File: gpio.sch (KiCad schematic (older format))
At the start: 33 parts, among them J3 Pro Bus, J7 PMOD1, J8 PMOD, SW1 SW_Push, SW2 SW_Push

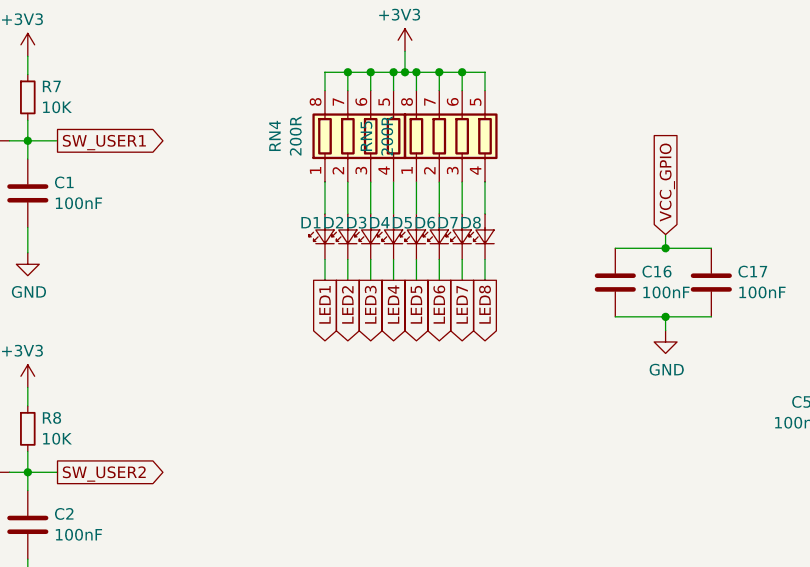
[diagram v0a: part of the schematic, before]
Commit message: component placement
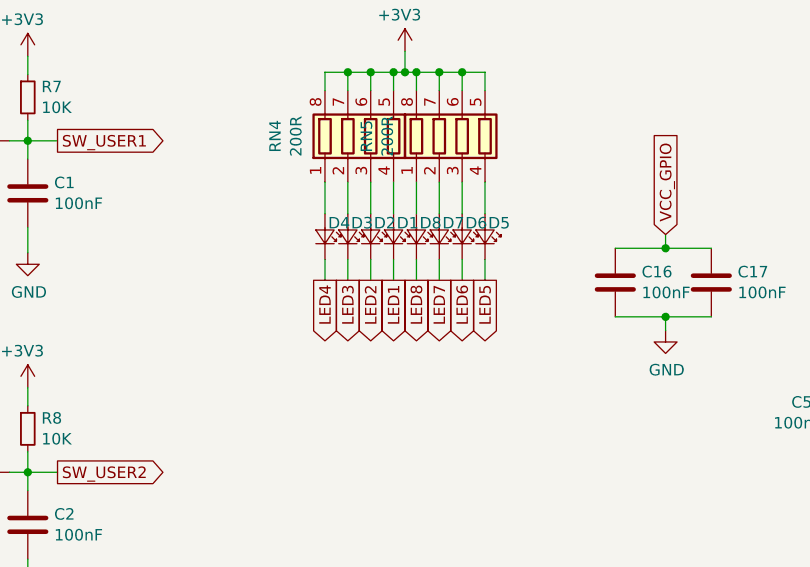
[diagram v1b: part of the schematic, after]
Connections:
- net at D5.2 (A): now also RN5.4 (R4.1); no longer RN5.1 (R1.1)
- net at D6.2 (A): now also RN5.3 (R3.1); no longer RN5.2 (R2.1)
- net at D7.2 (A): now also RN5.2 (R2.1); no longer RN5.3 (R3.1)
- net at D8.2 (A): now also RN5.1 (R1.1); no longer RN5.4 (R4.1)
- net at RN4.1 (R1.1): now also D4.2 (A); no longer D1.2 (A)
- net at RN4.2 (R2.1): now also D3.2 (A); no longer D2.2 (A)
- net at RN4.3 (R3.1): now also D2.2 (A); no longer D3.2 (A)
- net at RN4.4 (R4.1): now also D1.2 (A); no longer D4.2 (A)
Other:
- moved on the sheet: D1, D2, D3, D4, D5, D6, D7, D8
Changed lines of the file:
@@
 $Descr A4 11693 8268
 encoding utf-8
-Sheet 4 6
+Sheet 5 6
 Title ""
 Date ""
@@
 L Device:LED_Small D?
 U 1 1 5D1B162E
-P 3280 1720
+P 3580 1720
 AR Path="/5CFABACD/5D1B162E" Ref="D?"  Part="1"
 AR Path="/5CF9C1ED/5D1B162E" Ref="D5"  Part="1"
-F 0 "D5" V 3340 1830 50  0000 R CNN
+F 0 "D5" V 3640 1830 50  0000 R CNN
+F 1 "Blue" V 3535 1652 50  0001 R CNN
+F 2 "LED_SMD:LED_0603_1608Metric_Pad1.05x0.95mm_HandSolder" V 3580 1720 50  0001 C CNN
+F 3 "~" V 3580 1720 50  0001 C CNN
+	1    3580 1720
+	0    1    -1   0
+$EndComp
+$Comp
+L Device:LED_Small D?
+U 1 1 5D1B1634
+P 3480 1720
+AR Path="/5CFABACD/5D1B1634" Ref="D?"  Part="1"
+AR Path="/5CF9C1ED/5D1B1634" Ref="D6"  Part="1"
+F 0 "D6" V 3540 1830 50  0000 R CNN
+F 1 "Blue" V 3435 1652 50  0001 R CNN
+F 2 "LED_SMD:LED_0603_1608Metric_Pad1.05x0.95mm_HandSolder" V 3480 1720 50  0001 C CNN
+F 3 "~" V 3480 1720 50  0001 C CNN
+	1    3480 1720
+	0    1    -1   0
+$EndComp
+$Comp
+L Device:LED_Small D?
+U 1 1 5D1B163A
+P 3380 1720
+AR Path="/5CFABACD/5D1B163A" Ref="D?"  Part="1"
+AR Path="/5CF9C1ED/5D1B163A" Ref="D7"  Part="1"
+F 0 "D7" V 3440 1830 50  0000 R CNN
+F 1 "Blue" V 3335 1652 50  0001 R CNN
+F 2 "LED_SMD:LED_0603_1608Metric_Pad1.05x0.95mm_HandSolder" V 3380 1720 50  0001 C CNN
+F 3 "~" V 3380 1720 50  0001 C CNN
+	1    3380 1720
+	0    1    -1   0
+$EndComp
+$Comp
+L Device:LED_Small D?
+U 1 1 5D1B1640
+P 3280 1720
+AR Path="/5CFABACD/5D1B1640" Ref="D?"  Part="1"
+AR Path="/5CF9C1ED/5D1B1640" Ref="D8"  Part="1"
+F 0 "D8" V 3340 1830 50  0000 R CNN
 F 1 "Blue" V 3235 1652 50  0001 R CNN
 F 2 "LED_SMD:LED_0603_1608Metric_Pad1.05x0.95mm_HandSolder" V 3280 1720 50  0001 C CNN
 F 3 "~" V 3280 1720 50  0001 C CNN
 	1    3280 1720
-	0    -1   -1   0
-$EndComp
-$Comp
-L Device:LED_Small D?
-U 1 1 5D1B1634
-P 3380 1720
-AR Path="/5CFABACD/5D1B1634" Ref="D?"  Part="1"
-AR Path="/5CF9C1ED/5D1B1634" Ref="D6"  Part="1"
-F 0 "D6" V 3440 1830 50  0000 R CNN
-F 1 "Blue" V 3335 1652 50  0001 R CNN
-F 2 "LED_SMD:LED_0603_1608Metric_Pad1.05x0.95mm_HandSolder" V 3380 1720 50  0001 C CNN
-F 3 "~" V 3380 1720 50  0001 C CNN
-	1    3380 1720
-	0    -1   -1   0
-$EndComp
-$Comp
-L Device:LED_Small D?
-U 1 1 5D1B163A
-P 3480 1720
-AR Path="/5CFABACD/5D1B163A" Ref="D?"  Part="1"
-AR Path="/5CF9C1ED/5D1B163A" Ref="D7"  Part="1"
-F 0 "D7" V 3540 1830 50  0000 R CNN
-F 1 "Blue" V 3435 1652 50  0001 R CNN
-F 2 "LED_SMD:LED_0603_1608Metric_Pad1.05x0.95mm_HandSolder" V 3480 1720 50  0001 C CNN
-F 3 "~" V 3480 1720 50  0001 C CNN
-	1    3480 1720
-	0    -1   -1   0
-$EndComp
-$Comp
-L Device:LED_Small D?
-U 1 1 5D1B1640
-P 3580 1720
-AR Path="/5CFABACD/5D1B1640" Ref="D?"  Part="1"
-AR Path="/5CF9C1ED/5D1B1640" Ref="D8"  Part="1"
-F 0 "D8" V 3640 1830 50  0000 R CNN
-F 1 "Blue" V 3535 1652 50  0001 R CNN
-F 2 "LED_SMD:LED_0603_1608Metric_Pad1.05x0.95mm_HandSolder" V 3580 1720 50  0001 C CNN
-F 3 "~" V 3580 1720 50  0001 C CNN
-	1    3580 1720
-	0    -1   -1   0
+	0    1    -1   0
 $EndComp
 Wire Wire Line
@@
 Wire Wire Line
 	3580 1620 3580 1480
-Text GLabel 3180 1910 3    50   Output ~ 0
+Text GLabel 2880 1910 3    50   Output ~ 0
 LED4
 Wire Wire Line
-	3180 1820 3180 1910
+	2880 1820 2880 1910
+Text GLabel 3580 1910 3    50   Output ~ 0
+LED5
+Wire Wire Line
+	3580 1820 3580 1910
+Text GLabel 3480 1910 3    50   Output ~ 0
+LED6
+Wire Wire Line
+	3480 1820 3480 1910
+Text GLabel 3380 1910 3    50   Output ~ 0
+LED7
+Wire Wire Line
+	3380 1820 3380 1910
 Text GLabel 3280 1910 3    50   Output ~ 0
-LED5
+LED8
 Wire Wire Line
 	3280 1820 3280 1910
-Text GLabel 3380 1910 3    50   Output ~ 0
-LED6
-Wire Wire Line
-	3380 1820 3380 1910
-Text GLabel 3480 1910 3    50   Output ~ 0
-LED7
-Wire Wire Line
-	3480 1820 3480 1910
-Text GLabel 3580 1910 3    50   Output ~ 0
-LED8
-Wire Wire Line
-	3580 1820 3580 1910
 Wire Wire Line
 	3580 1000 3580 1080
@@
 	2880 1080 2880 1000
 Wire Wire Line
+	2980 1820 2980 1910
+Text GLabel 2980 1910 3    50   Output ~ 0
+LED3
+Wire Wire Line
 	3080 1820 3080 1910
 Text GLabel 3080 1910 3    50   Output ~ 0
-LED3
-Wire Wire Line
-	2980 1820 2980 1910
-Text GLabel 2980 1910 3    50   Output ~ 0
 LED2
 Wire Wire Line
-	2880 1820 2880 1910
-Text GLabel 2880 1910 3    50   Output ~ 0
+	3180 1820 3180 1910
+Text GLabel 3180 1910 3    50   Output ~ 0
 LED1
 Wire Wire Line
@@
 L Device:LED_Small D?
 U 1 1 5D1B16E7
-P 3180 1720
+P 2880 1720
 AR Path="/5CFABACD/5D1B16E7" Ref="D?"  Part="1"
 AR Path="/5CF9C1ED/5D1B16E7" Ref="D4"  Part="1"
-F 0 "D4" V 3240 1830 50  0000 R CNN
+F 0 "D4" V 2940 1830 50  0000 R CNN
+F 1 "Blue" V 2835 1652 50  0001 R CNN
+F 2 "LED_SMD:LED_0603_1608Metric_Pad1.05x0.95mm_HandSolder" V 2880 1720 50  0001 C CNN
+F 3 "~" V 2880 1720 50  0001 C CNN
+	1    2880 1720
+	0    1    -1   0
+$EndComp
+$Comp
+L Device:LED_Small D?
+U 1 1 5D1B16ED
+P 2980 1720
+AR Path="/5CFABACD/5D1B16ED" Ref="D?"  Part="1"
+AR Path="/5CF9C1ED/5D1B16ED" Ref="D3"  Part="1"
+F 0 "D3" V 3040 1830 50  0000 R CNN
+F 1 "Blue" V 2935 1652 50  0001 R CNN
+F 2 "LED_SMD:LED_0603_1608Metric_Pad1.05x0.95mm_HandSolder" V 2980 1720 50  0001 C CNN
+F 3 "~" V 2980 1720 50  0001 C CNN
+	1    2980 1720
+	0    1    -1   0
+$EndComp
+$Comp
+L Device:LED_Small D?
+U 1 1 5D1B16F3
+P 3080 1720
+AR Path="/5CFABACD/5D1B16F3" Ref="D?"  Part="1"
+AR Path="/5CF9C1ED/5D1B16F3" Ref="D2"  Part="1"
+F 0 "D2" V 3140 1830 50  0000 R CNN
+F 1 "Blue" V 3035 1652 50  0001 R CNN
+F 2 "LED_SMD:LED_0603_1608Metric_Pad1.05x0.95mm_HandSolder" V 3080 1720 50  0001 C CNN
+F 3 "~" V 3080 1720 50  0001 C CNN
+	1    3080 1720
+	0    1    -1   0
+$EndComp
+$Comp
+L Device:LED_Small D?
+U 1 1 5D1B16F9
+P 3180 1720
+AR Path="/5CFABACD/5D1B16F9" Ref="D?"  Part="1"
+AR Path="/5CF9C1ED/5D1B16F9" Ref="D1"  Part="1"
+F 0 "D1" V 3240 1830 50  0000 R CNN
 F 1 "Blue" V 3135 1652 50  0001 R CNN
 F 2 "LED_SMD:LED_0603_1608Metric_Pad1.05x0.95mm_HandSolder" V 3180 1720 50  0001 C CNN
 F 3 "~" V 3180 1720 50  0001 C CNN
 	1    3180 1720
-	0    -1   -1   0
-$EndComp
-$Comp
-L Device:LED_Small D?
-U 1 1 5D1B16ED
-P 3080 1720
-AR Path="/5CFABACD/5D1B16ED" Ref="D?"  Part="1"
-AR Path="/5CF9C1ED/5D1B16ED" Ref="D3"  Part="1"
-F 0 "D3" V 3140 1830 50  0000 R CNN
-F 1 "Blue" V 3035 1652 50  0001 R CNN
-F 2 "LED_SMD:LED_0603_1608Metric_Pad1.05x0.95mm_HandSolder" V 3080 1720 50  0001 C CNN
-F 3 "~" V 3080 1720 50  0001 C CNN
-	1    3080 1720
-	0    -1   -1   0
-$EndComp
-$Comp
-L Device:LED_Small D?
-U 1 1 5D1B16F3
-P 2980 1720
-AR Path="/5CFABACD/5D1B16F3" Ref="D?"  Part="1"
-AR Path="/5CF9C1ED/5D1B16F3" Ref="D2"  Part="1"
-F 0 "D2" V 3040 1830 50  0000 R CNN
-F 1 "Blue" V 2935 1652 50  0001 R CNN
-F 2 "LED_SMD:LED_0603_1608Metric_Pad1.05x0.95mm_HandSolder" V 2980 1720 50  0001 C CNN
-F 3 "~" V 2980 1720 50  0001 C CNN
-	1    2980 1720
-	0    -1   -1   0
-$EndComp
-$Comp
-L Device:LED_Small D?
-U 1 1 5D1B16F9
-P 2880 1720
-AR Path="/5CFABACD/5D1B16F9" Ref="D?"  Part="1"
-AR Path="/5CF9C1ED/5D1B16F9" Ref="D1"  Part="1"
-F 0 "D1" V 2940 1830 50  0000 R CNN
-F 1 "Blue" V 2835 1652 50  0001 R CNN
-F 2 "LED_SMD:LED_0603_1608Metric_Pad1.05x0.95mm_HandSolder" V 2880 1720 50  0001 C CNN
-F 3 "~" V 2880 1720 50  0001 C CNN
-	1    2880 1720
-	0    -1   -1   0
+	0    1    -1   0
 $EndComp
 Text GLabel 10170 1990 2    50   Input ~ 0

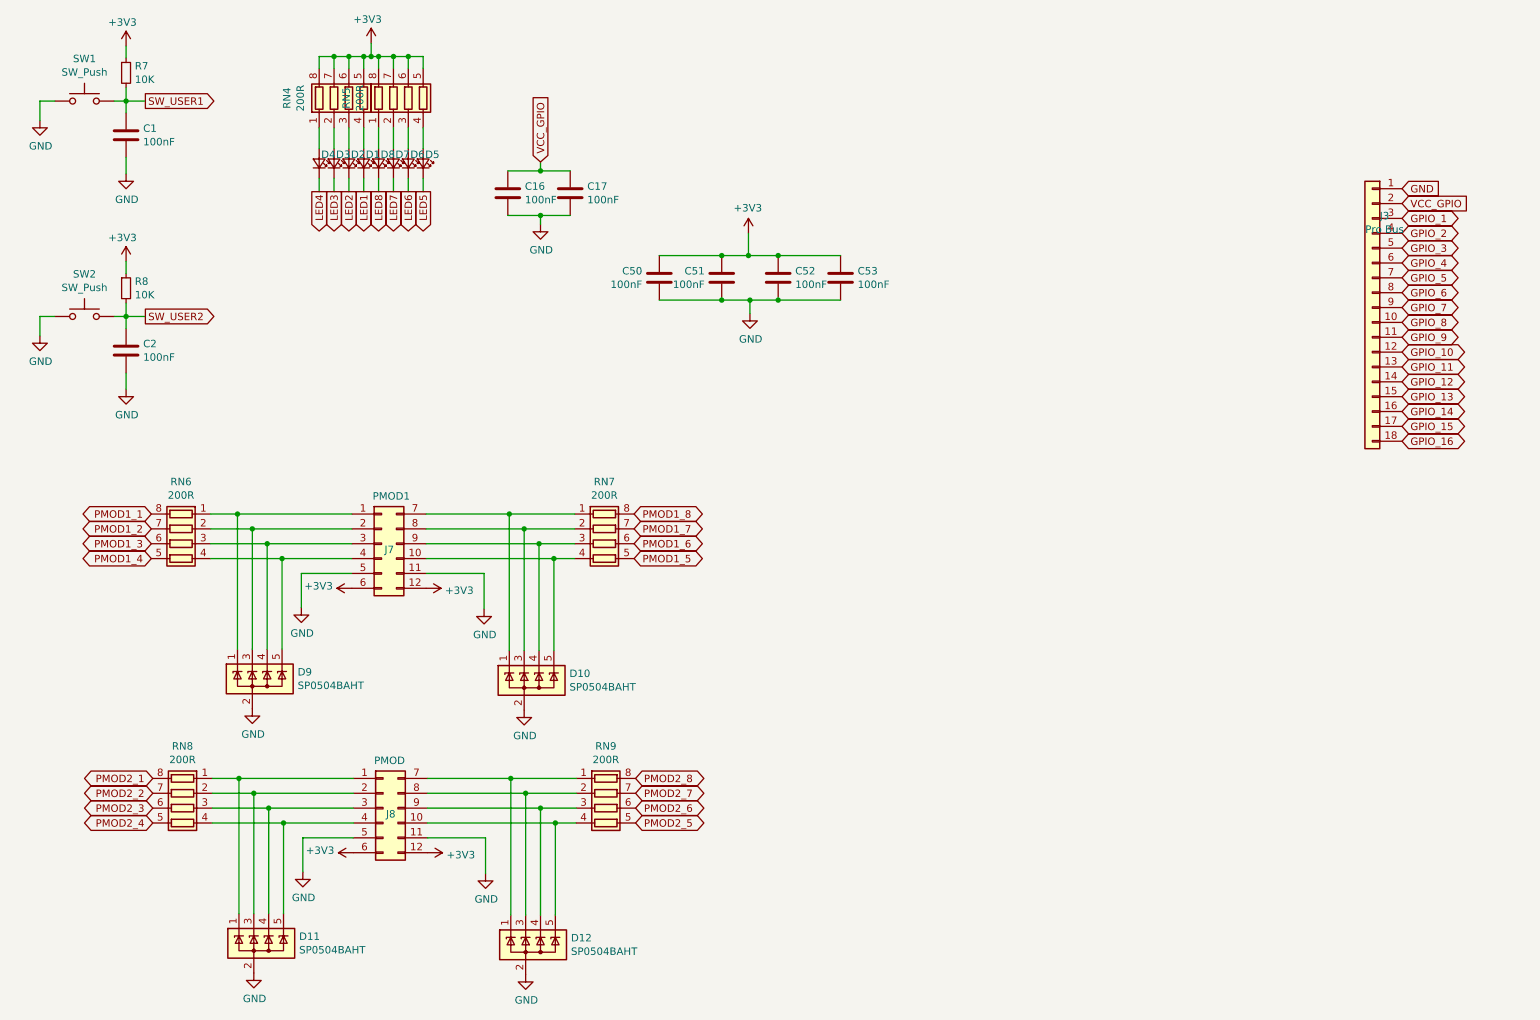
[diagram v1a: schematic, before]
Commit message: organized bypass caps
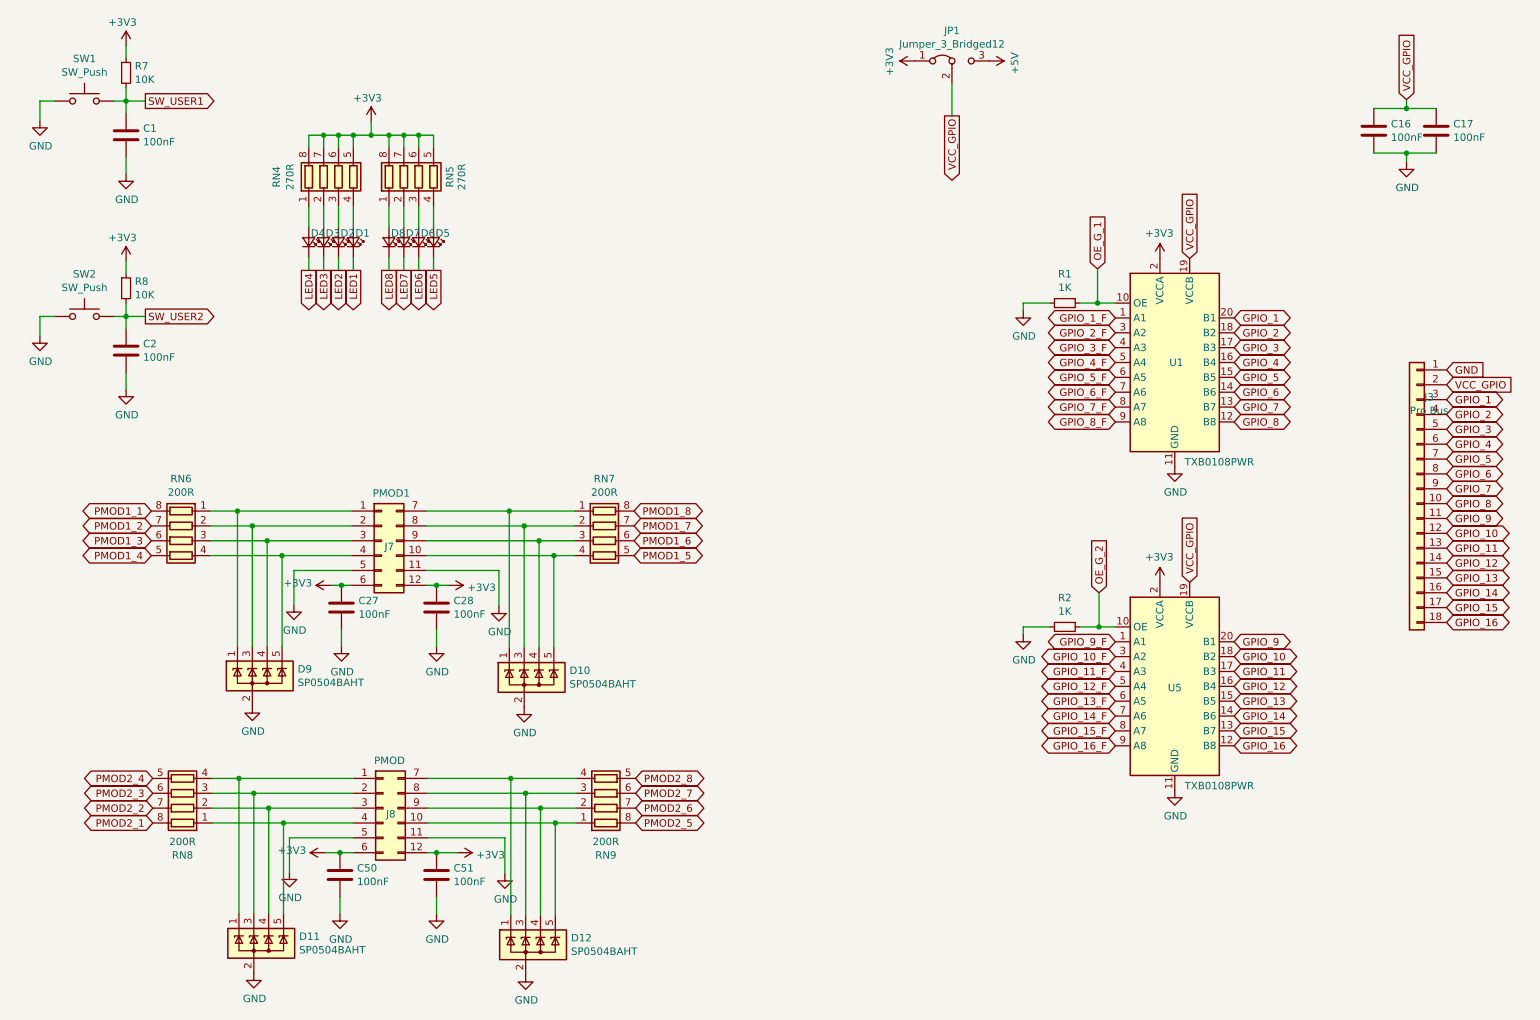
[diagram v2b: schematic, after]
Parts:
- removed C52, C53: 100nF, Capacitor_SMD:C_0603_1608Metric_Pad1.05x0.95mm_HandSolder, symbol Device:C
- added C27, C28: 100nF, Capacitor_SMD:C_0603_1608Metric_Pad1.05x0.95mm_HandSolder, symbol Device:C
- added JP1: Jumper_3_Bridged12, Connector_PinHeader_2.54mm:PinHeader_1x03_P2.54mm_Vertical, symbol Jumper:Jumper_3_Bridged12
- added R1, R2: 1K, Resistor_SMD:R_0603_1608Metric_Pad1.05x0.95mm_HandSolder, symbol Device:R_Small
- added U1, U5: TXB0108PWR, Package_SO:TSSOP-20_4.4x6.5mm_P0.65mm, symbol rc2014_max_v-rescue:TXB0108PWR-Logic_LevelTranslator
- RN4, RN5: value 200R -> 270R
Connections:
- net +3V3: now also C27.1, C28.1, JP1.1 (A), U1.2 (VCCA), U5.2 (VCCA)
- net GND: now also C27.2, C28.2, R1.2, R2.2, U1.11 (GND), U5.11 (GND)
- net GPIO_1: now also U1.20 (B1)
- net GPIO_10: now also U5.18 (B2)
- net GPIO_11: now also U5.17 (B3)
- net GPIO_12: now also U5.16 (B4)
- net GPIO_13: now also U5.15 (B5)
- net GPIO_14: now also U5.14 (B6)
- net GPIO_15: now also U5.13 (B7)
- net GPIO_16: now also U5.12 (B8)
- net GPIO_2: now also U1.18 (B2)
- net GPIO_3: now also U1.17 (B3)
- net GPIO_4: now also U1.16 (B4)
- net GPIO_5: now also U1.15 (B5)
- net GPIO_6: now also U1.14 (B6)
- net GPIO_7: now also U1.13 (B7)
- net GPIO_8: now also U1.12 (B8)
- net GPIO_9: now also U5.20 (B1)
- net PMOD2_5: now also RN9.8 (R1.2); no longer RN9.5 (R4.2)
- net PMOD2_6: now also RN9.7 (R2.2); no longer RN9.6 (R3.2)
- net PMOD2_7: now also RN9.6 (R3.2); no longer RN9.7 (R2.2)
- net PMOD2_8: now also RN9.5 (R4.2); no longer RN9.8 (R1.2)
- net VCC_GPIO: now also JP1.2 (C), U1.19 (VCCB), U5.19 (VCCB)
- net at D11.1 (K), J8.1 (Pin_1): now also RN8.4 (R4.1); no longer RN8.1 (R1.1)
- net at D11.3 (K), J8.2 (Pin_2): now also RN8.3 (R3.1); no longer RN8.2 (R2.1)
- net at D11.4 (K), J8.3 (Pin_3): now also RN8.2 (R2.1); no longer RN8.3 (R3.1)
- net at D11.5 (K), J8.4 (Pin_4): now also RN8.1 (R1.1); no longer RN8.4 (R4.1)
- net at D12.1 (K), J8.7 (Pin_7): now also RN9.4 (R4.1); no longer RN9.1 (R1.1)
- net at D12.3 (K), J8.8 (Pin_8): now also RN9.3 (R3.1); no longer RN9.2 (R2.1)
- net at D12.4 (K), J8.9 (Pin_9): now also RN9.2 (R2.1); no longer RN9.3 (R3.1)
- net at D12.5 (K), J8.10 (Pin_10): now also RN9.1 (R1.1); no longer RN9.4 (R4.1)
- new net +5V: JP1.3 (B)
- new net GPIO_10_F: U5.3 (A2)
- new net GPIO_11_F: U5.4 (A3)
- new net GPIO_12_F: U5.5 (A4)
- new net GPIO_13_F: U5.6 (A5)
- new net GPIO_14_F: U5.7 (A6)
- new net GPIO_15_F: U5.8 (A7)
- new net GPIO_16_F: U5.9 (A8)
- new net GPIO_1_F: U1.1 (A1)
- new net GPIO_2_F: U1.3 (A2)
- new net GPIO_3_F: U1.4 (A3)
- new net GPIO_4_F: U1.5 (A4)
- new net GPIO_5_F: U1.6 (A5)
- new net GPIO_6_F: U1.7 (A6)
- new net GPIO_7_F: U1.8 (A7)
- new net GPIO_8_F: U1.9 (A8)
- new net GPIO_9_F: U5.1 (A1)
- new net OE_G_1: R1.1, U1.10 (OE)
- new net OE_G_2: R2.1, U5.10 (OE)
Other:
- moved on the sheet: C16, C17, D1, D10, D2, D3, D4, D5, D6, D7, D8, D9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

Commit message: fixed errors, connected all pins, switched to 4 layers
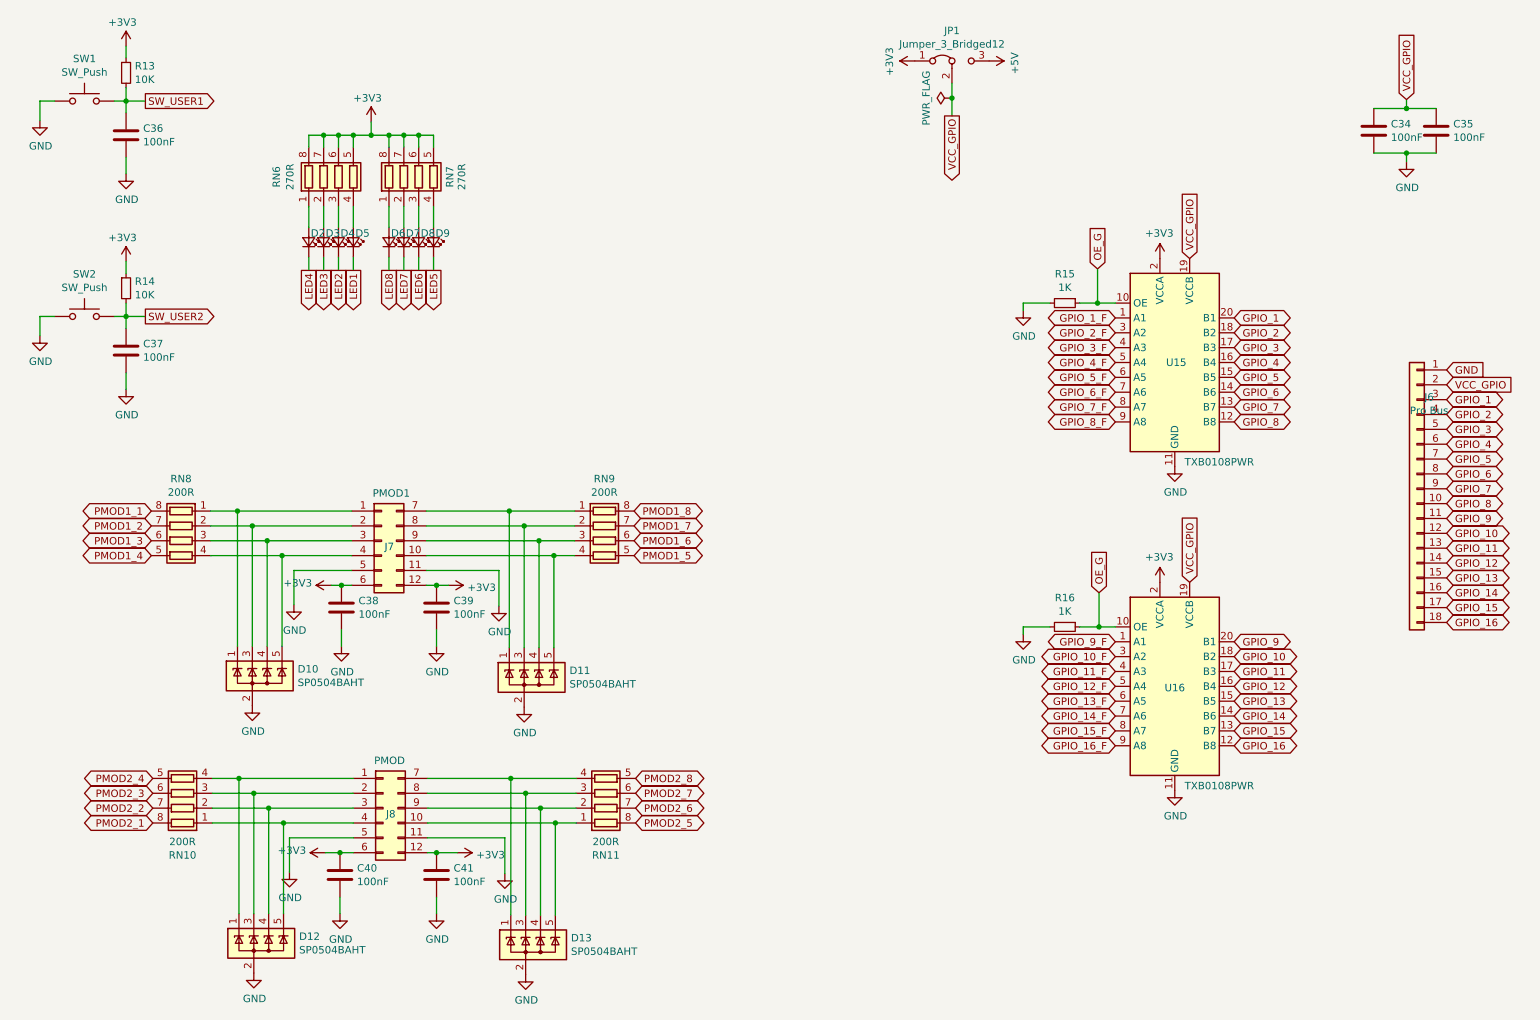
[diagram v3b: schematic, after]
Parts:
- renumbered C16 to C34, C17 to C35, C1 to C36, C2 to C37, C27 to C38, C28 to C39, C50 to C40, C51 to C41, D9 to D10, D10 to D11, D11 to D12, D12 to D13, D4 to D2, D2 to D4, D1 to D5, D8 to D6, D6 to D8, D5 to D9, J3 to J6, R7 to R13, R8 to R14, R1 to R15, R2 to R16, RN8 to RN10, RN9 to RN11, RN4 to RN6, RN5 to RN7, RN6 to RN8, RN7 to RN9, U1 to U15, U5 to U16
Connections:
- net OE_G_2 is gone; now on net OE_G: R16.1, U16.10 (OE)
- net OE_G_1 renamed OE_G
